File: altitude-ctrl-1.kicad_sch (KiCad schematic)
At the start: 19 parts, among them J5 Conn_01x04_Pin, U4 STM32F103C8Tx, Y1 8M

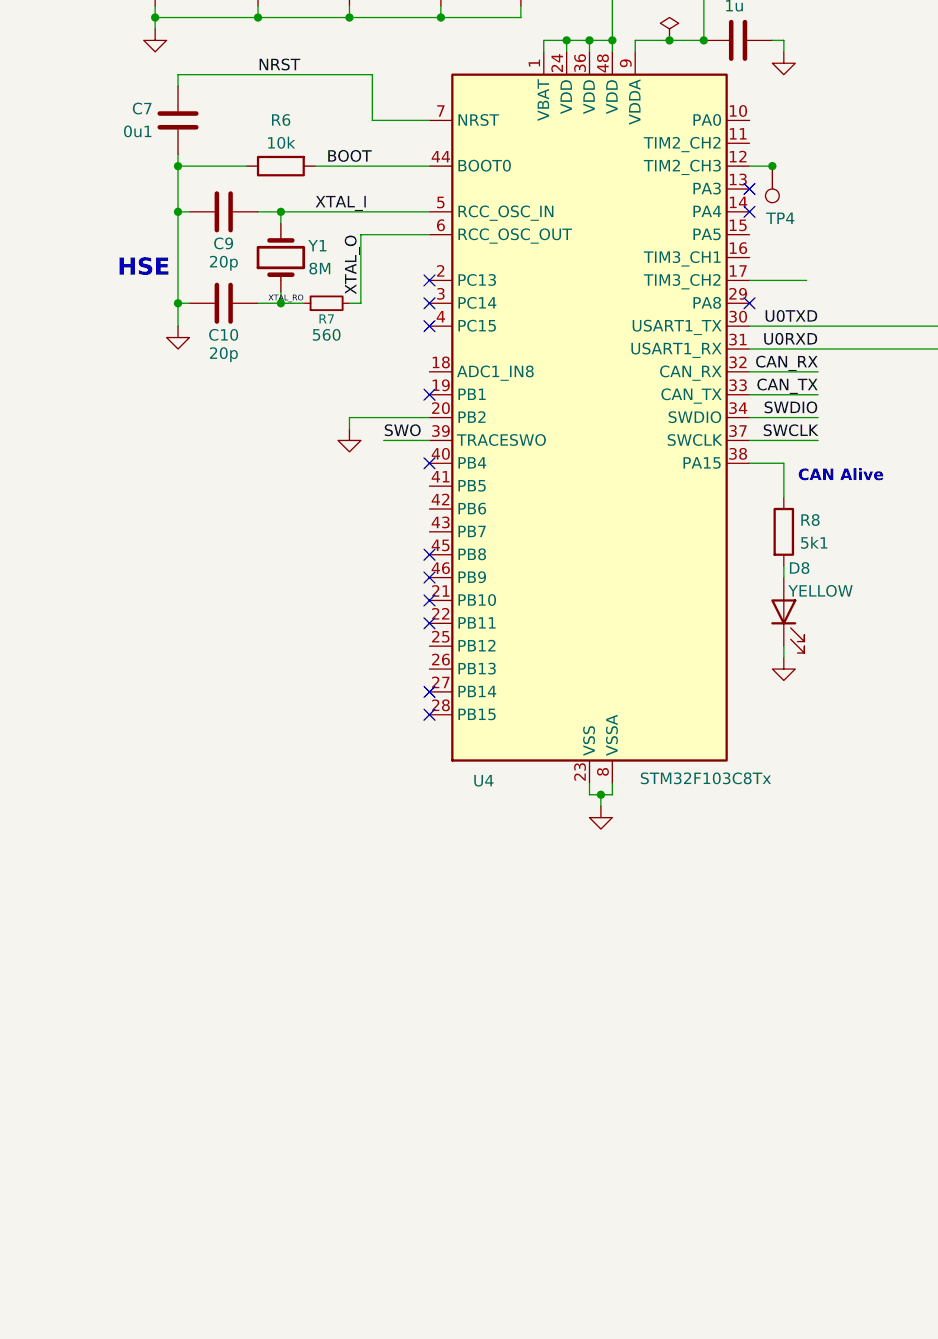
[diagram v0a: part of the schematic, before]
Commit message: schem: import ldo, mnt holes, ldo, btns and fiducials
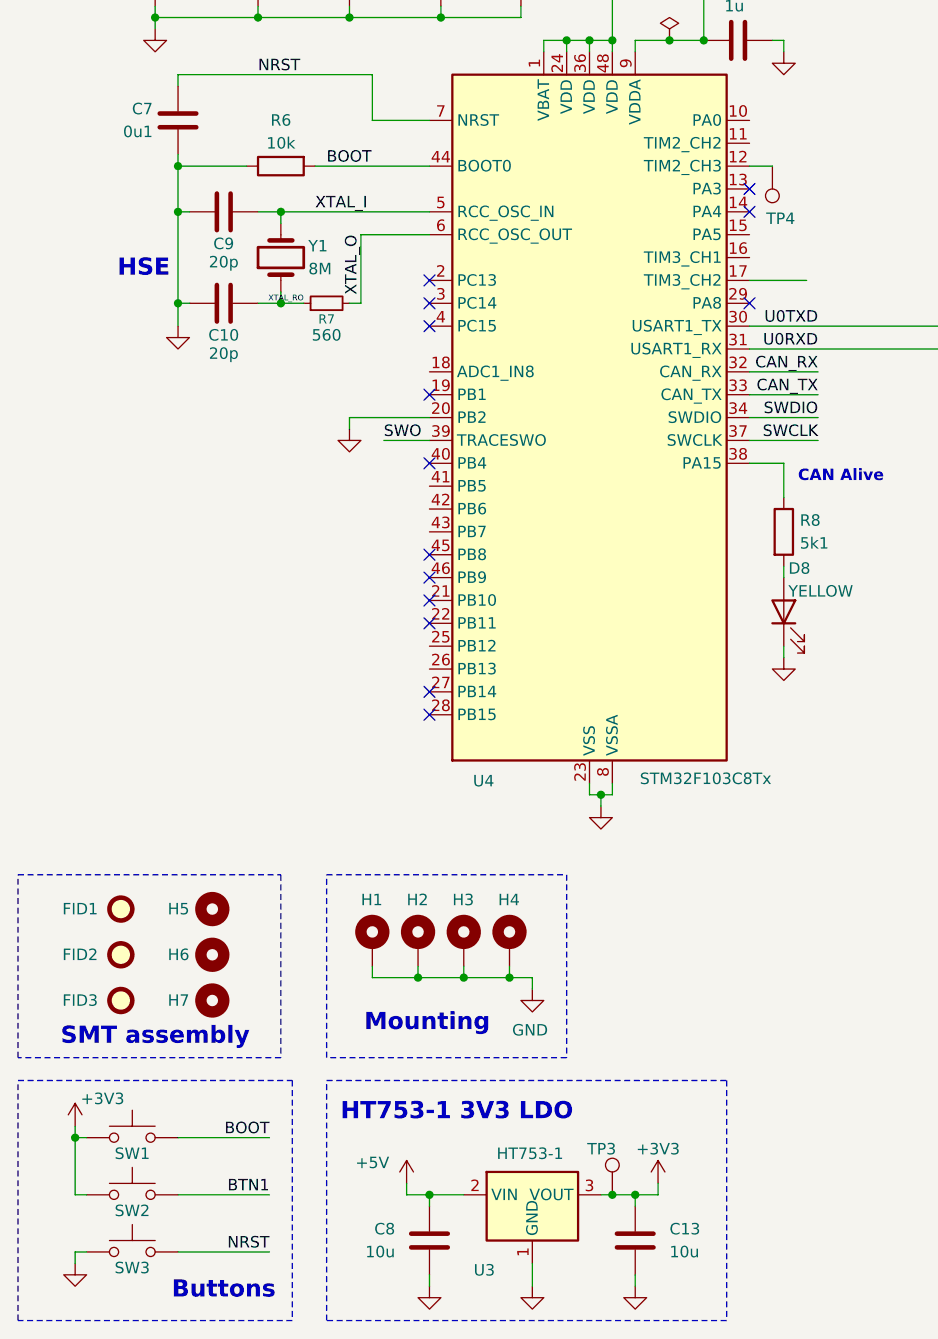
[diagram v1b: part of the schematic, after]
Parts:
- added C13, C8: 10u, Capacitor_SMD:C_0805_2012Metric, symbol Device:C
- added FID1, FID2, FID3: Fiducial, Fiducial:Fiducial_1mm_Mask2mm, symbol Mechanical:Fiducial
- added H1, H2, H3, H4: MountingHole_Pad, MountingHole:MountingHole_3.2mm_M3_Pad_Via, symbol Mechanical:MountingHole_Pad
- added H5, H6, H7: MountingHole, MountingHole:ToolingHole_1.152mm, symbol Mechanical:MountingHole
- added SW1, SW2, SW3: SW_Push, Button_Switch_SMD:SW_SPST_TS-1088-xR020, symbol Switch:SW_Push
- added TP3: TestPoint, TestPoint:TestPoint_Pad_D2.0mm, symbol Connector:TestPoint
- added U3: HT753-1, Package_TO_SOT_SMD:SOT-89-3, symbol Regulator_Linear:HT75xx-1-SOT89
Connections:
- net +3V3: now also C13.1, SW1.1, SW2.1, TP3.1, U3.3 (VOUT)
- net BOOT: now also SW1.2
- net GND: now also C13.2, C8.2, H1.1, H2.1, H3.1, H4.1, SW3.1, U3.1 (GND)
- net NRST: now also SW3.2
- new net +5V: C8.1, U3.2 (VIN)
- new net BTN1: SW2.2
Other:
- note added: "Buttons"
- note added: "HT753-1 3V3 LDO"
- note added: "Mounting"
- note added: "SMT assembly"

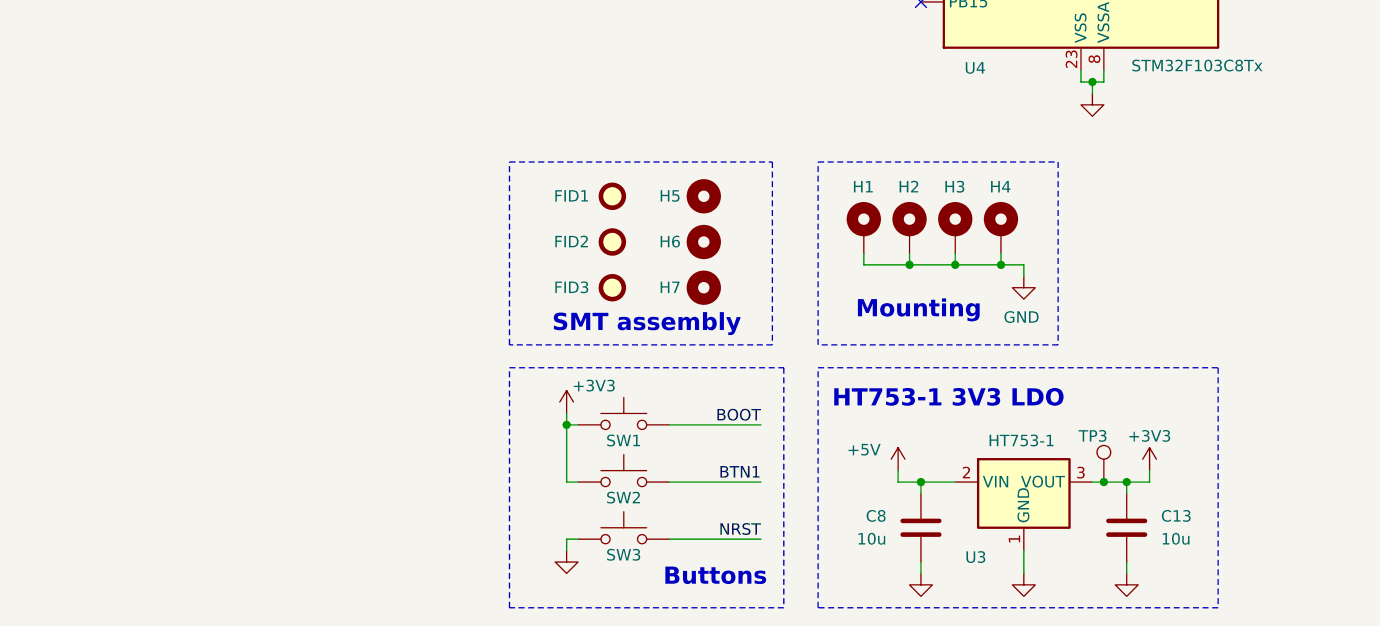
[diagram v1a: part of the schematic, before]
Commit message: schem: import tag connect swd
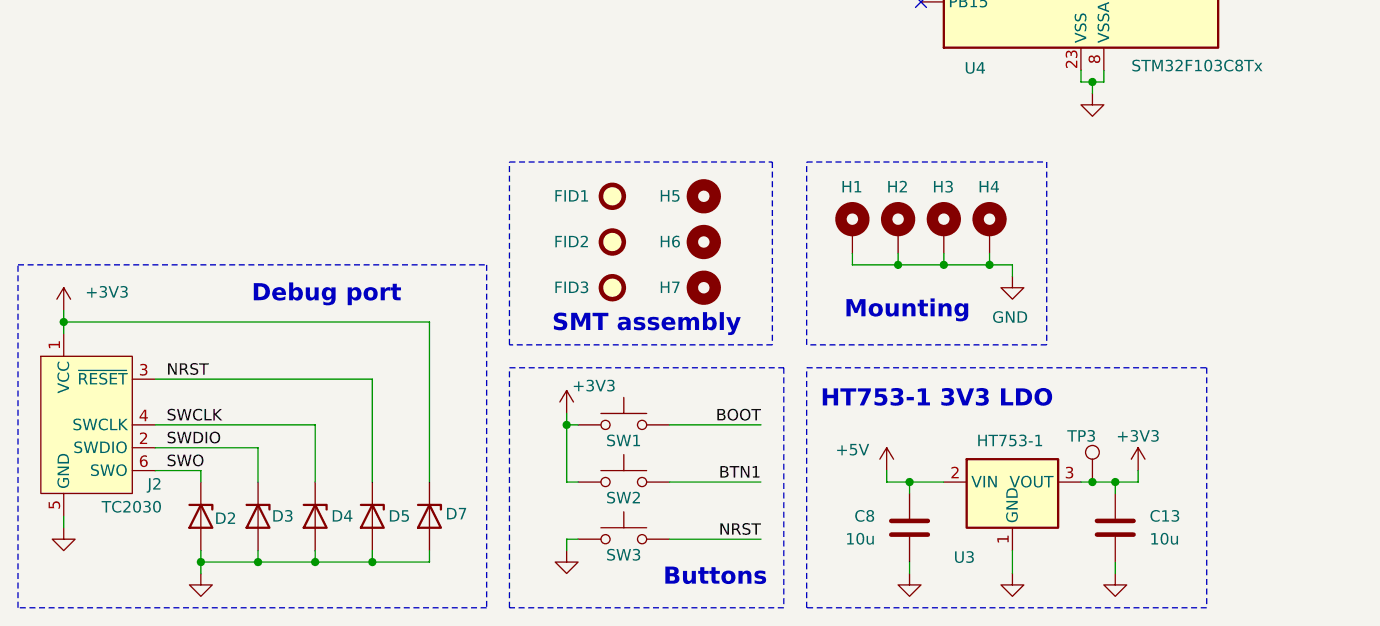
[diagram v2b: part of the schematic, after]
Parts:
- added D2, D3, D4, D5, D7: H5VU10U, GLCS:Diode_DFN1006, symbol GLCS:H5VU10U
- added J2: TC2030, Connector:Tag-Connect_TC2030-IDC-NL_2x03_P1.27mm_Vertical, symbol Connector:Conn_ARM_SWD_TagConnect_TC2030-NL
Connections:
- net +3V3: now also D7.1 (K), J2.1 (VCC)
- net GND: now also D2.2 (A), D3.2 (A), D4.2 (A), D5.2 (A), D7.2 (A), J2.5 (GND)
- net NRST: now also D5.1 (K), J2.3 (~{RESET})
- net SWCLK: now also D4.1 (K), J2.4 (SWCLK)
- net SWDIO: now also D3.1 (K), J2.2 (SWDIO)
- net SWO: now also D2.1 (K), J2.6 (SWO)
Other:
- note added: "Debug port"
- moved on the sheet: C13, C8, H1, H2, H3, H4, TP3, U3

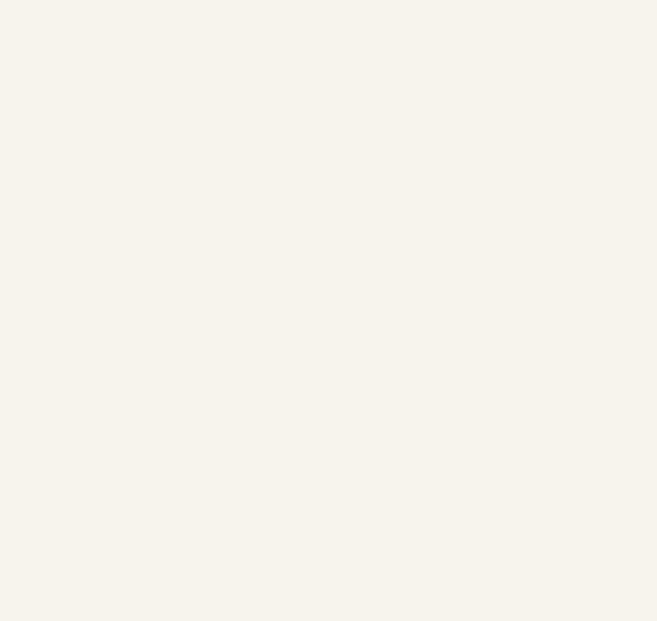
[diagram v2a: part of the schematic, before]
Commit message: schem: import can transceiver
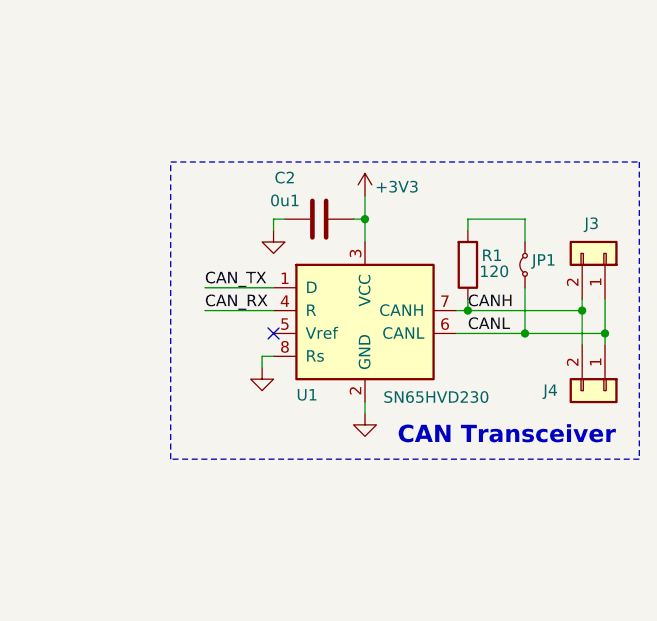
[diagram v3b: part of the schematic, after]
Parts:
- added C2: 0u1, Capacitor_SMD:C_0402_1005Metric, symbol Device:C
- added J3, J4: Conn_01x02, Connector_JST:JST_XH_B2B-XH-A_1x02_P2.50mm_Vertical, symbol Connector_Generic:Conn_01x02
- added JP1: Jumper_2_Small_Bridged, Connector_PinHeader_2.54mm:PinHeader_1x02_P2.54mm_Vertical, symbol Jumper:Jumper_2_Small_Bridged
- added R1: 120, Resistor_SMD:R_1206_3216Metric, symbol Device:R
- added U1: SN65HVD230, Package_SO:SOIC-8_3.9x4.9mm_P1.27mm, symbol Interface_CAN_LIN:SN65HVD230
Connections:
- net +3V3: now also C2.1, U1.3 (VCC)
- net CAN_RX: now also U1.4 (R)
- net CAN_TX: now also U1.1 (D)
- net GND: now also C2.2, U1.2 (GND), U1.8 (Rs)
- new net: JP1.2 (B), R1.2
- new net CANH: J3.2 (Pin_2), J4.2 (Pin_2), R1.1, U1.7 (CANH)
- new net CANL: J3.1 (Pin_1), J4.1 (Pin_1), JP1.1 (A), U1.6 (CANL)
- no-connect marks 14 -> 15
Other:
- note added: "CAN Transceiver"

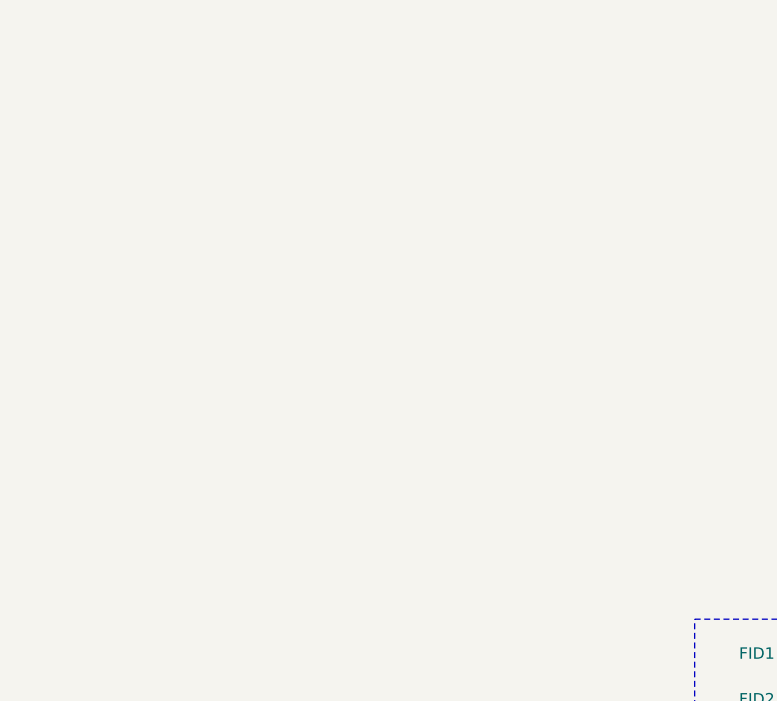
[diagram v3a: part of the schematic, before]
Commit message: schem: import LM73100 Ideal diode
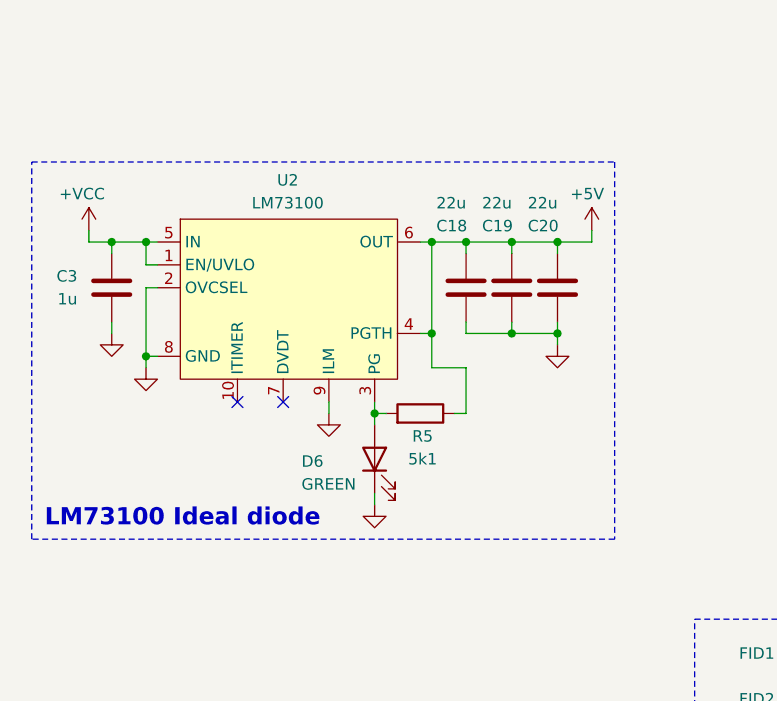
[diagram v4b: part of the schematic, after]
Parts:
- added C18, C19, C20: 22u, Capacitor_SMD:C_0805_2012Metric, symbol Device:C
- added C3: 1u, Capacitor_SMD:C_0402_1005Metric, symbol Device:C
- added D6: GREEN, LED_SMD:LED_0805_2012Metric, symbol Device:LED
- added R5: 5k1, Resistor_SMD:R_0402_1005Metric, symbol Device:R
- added U2: LM73100, GLCS:Texas_RPW0010A_VQFN-HR-10_2x2mm_P0.5mm, symbol GLCS:LM73100
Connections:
- net +5V: now also C18.2, C19.2, C20.2, R5.1, U2.4 (PGTH), U2.6 (OUT)
- net GND: now also C18.1, C19.1, C20.1, C3.1, D6.1 (K), U2.2 (OVCSEL), U2.8 (GND), U2.9 (ILM)
- new net: D6.2 (A), R5.2, U2.3 (PG)
- new net +VCC: C3.2, U2.1 (EN/UVLO), U2.5 (IN)
- no-connect marks 15 -> 17
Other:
- note added: "LM73100 Ideal diode"

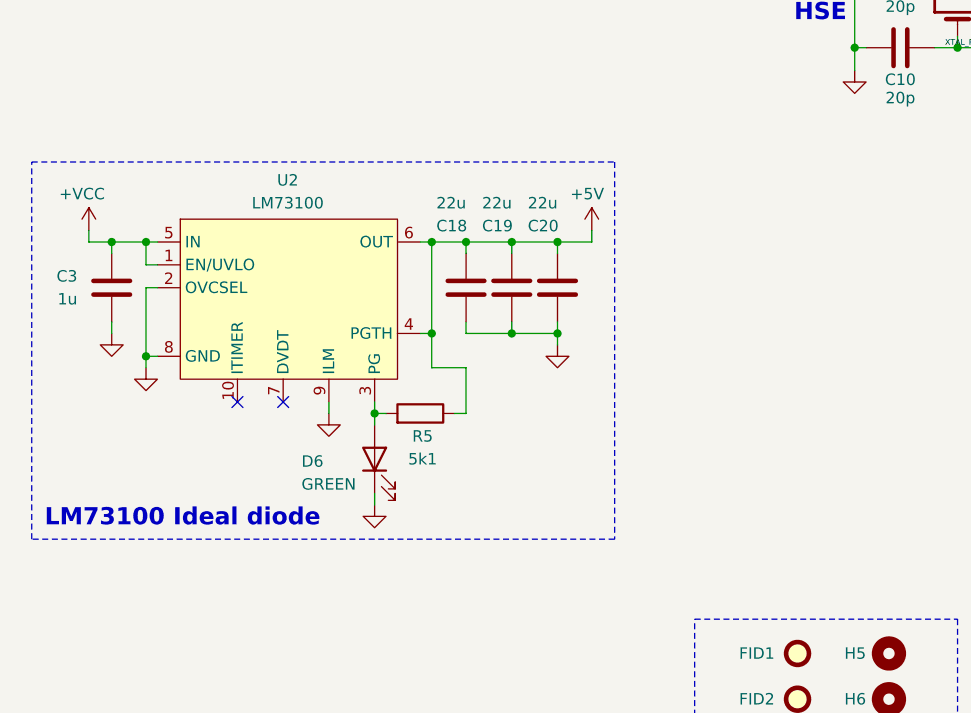
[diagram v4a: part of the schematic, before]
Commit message: schem: add LM73100 Ideal diode ov protection
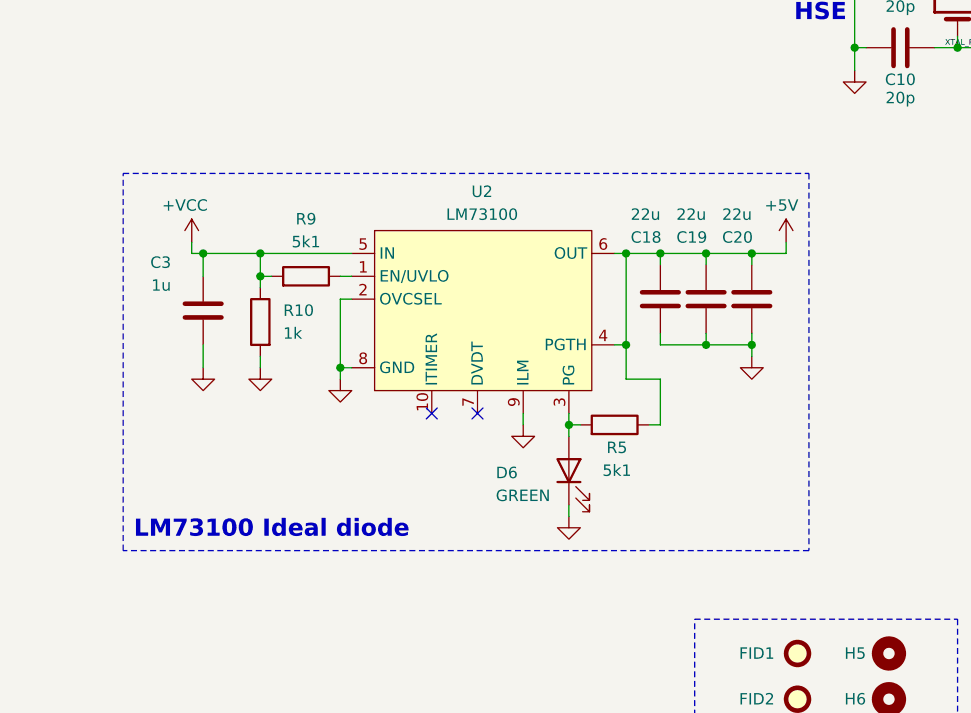
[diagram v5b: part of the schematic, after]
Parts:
- added R10: 1k, Resistor_SMD:R_0402_1005Metric, symbol Device:R
- added R9: 5k1, Resistor_SMD:R_0402_1005Metric, symbol Device:R
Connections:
- net +VCC: now also R10.1, R9.2; no longer U2.1 (EN/UVLO)
- net GND: now also R10.2
- new net: R9.1, U2.1 (EN/UVLO)
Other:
- moved on the sheet: C18, C19, C20, C3, D6, R5, U2

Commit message: schem: add LM73100 +12V input protection
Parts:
- added C21, C22, C23: 22u, Capacitor_SMD:C_0805_2012Metric, symbol Device:C
- added C4: 1u, Capacitor_SMD:C_0402_1005Metric, symbol Device:C
- added D9: GREEN, LED_SMD:LED_0805_2012Metric, symbol Device:LED
- added R11: 1k, Resistor_SMD:R_0402_1005Metric, symbol Device:R
- added R12: 10k, Resistor_SMD:R_0402_1005Metric, symbol Device:R
- added R13: 5k1, Resistor_SMD:R_0402_1005Metric, symbol Device:R
- added U5: LM73100, GLCS:Texas_RPW0010A_VQFN-HR-10_2x2mm_P0.5mm, symbol GLCS:LM73100
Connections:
- net GND: now also C21.1, C22.1, C23.1, C4.1, D9.1 (K), R11.2, U5.2 (OVCSEL), U5.8 (GND), U5.9 (ILM)
- new net: R12.2, U5.1 (EN/UVLO)
- new net: D9.2 (A), R13.2, U5.3 (PG)
- new net +12V: C21.2, C22.2, C23.2, R13.1, U5.4 (PGTH), U5.6 (OUT)
- new net +12V_IN: C4.2, R11.1, R12.1, U5.5 (IN)
- no-connect marks 17 -> 19
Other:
- note added: "LM73100 12V Input protection"
- note added: "LM73100 5V Input protection"
- note removed: "LM73100 Ideal diode"
